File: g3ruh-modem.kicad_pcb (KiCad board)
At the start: 2 copper layers, 160 x 100 mm, 112 parts, among them P1 CONN_01X03, P2 CONN_01X06, P3 CONN_01X05, P4 C96ABC, Q1 LM7805_TO220, U1 4029, U10 LM339, U11 74HC14, U12 74HC164, U13 74HC86, U14 74HC164, U15 27C128, U16 TL084, U17 74HC74, U18 74HC164, U19 ZN429E-8, U2 27C128, U3 4029, U4 74HC164, U5 74HC74, U6 74HC86, U7 74HC164, U8 74HC161, U9 ZN429E-8

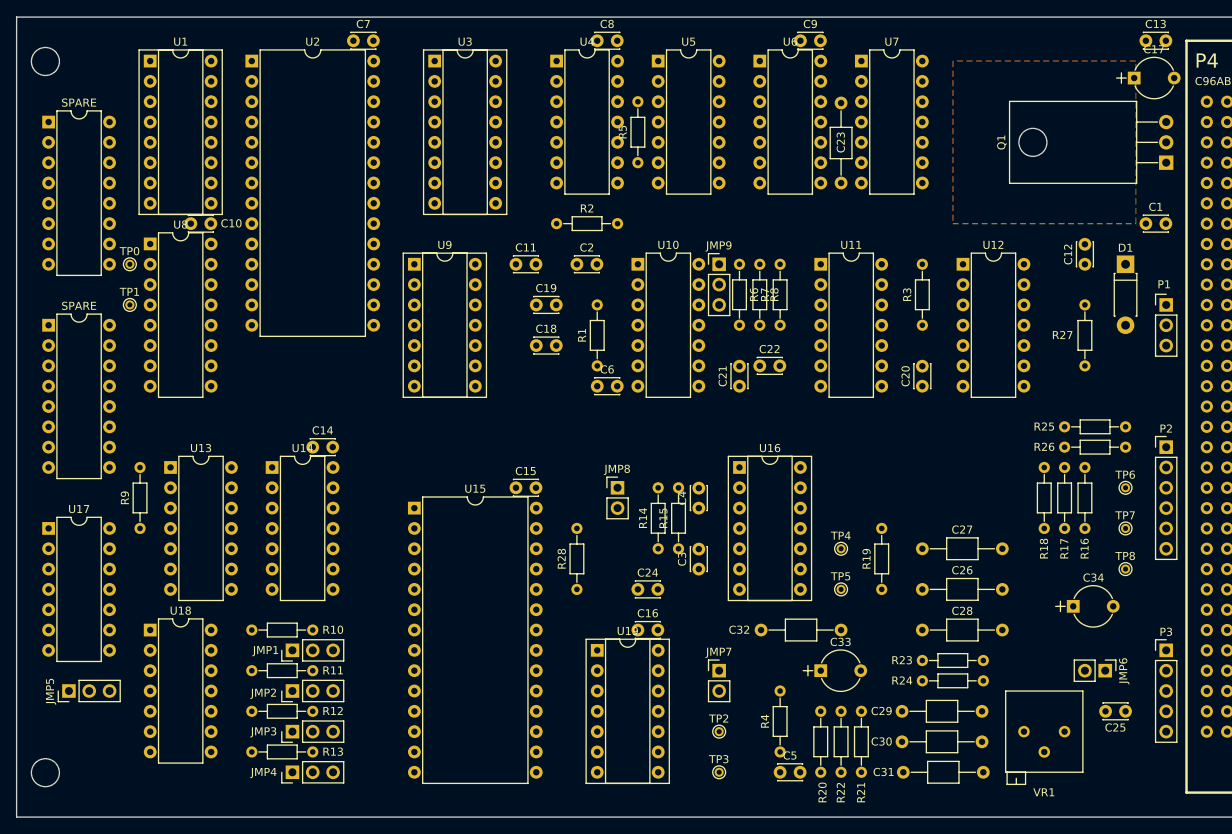
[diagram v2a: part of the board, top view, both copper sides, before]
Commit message: Final parts placement and verified net against an actual Issue 3 board.
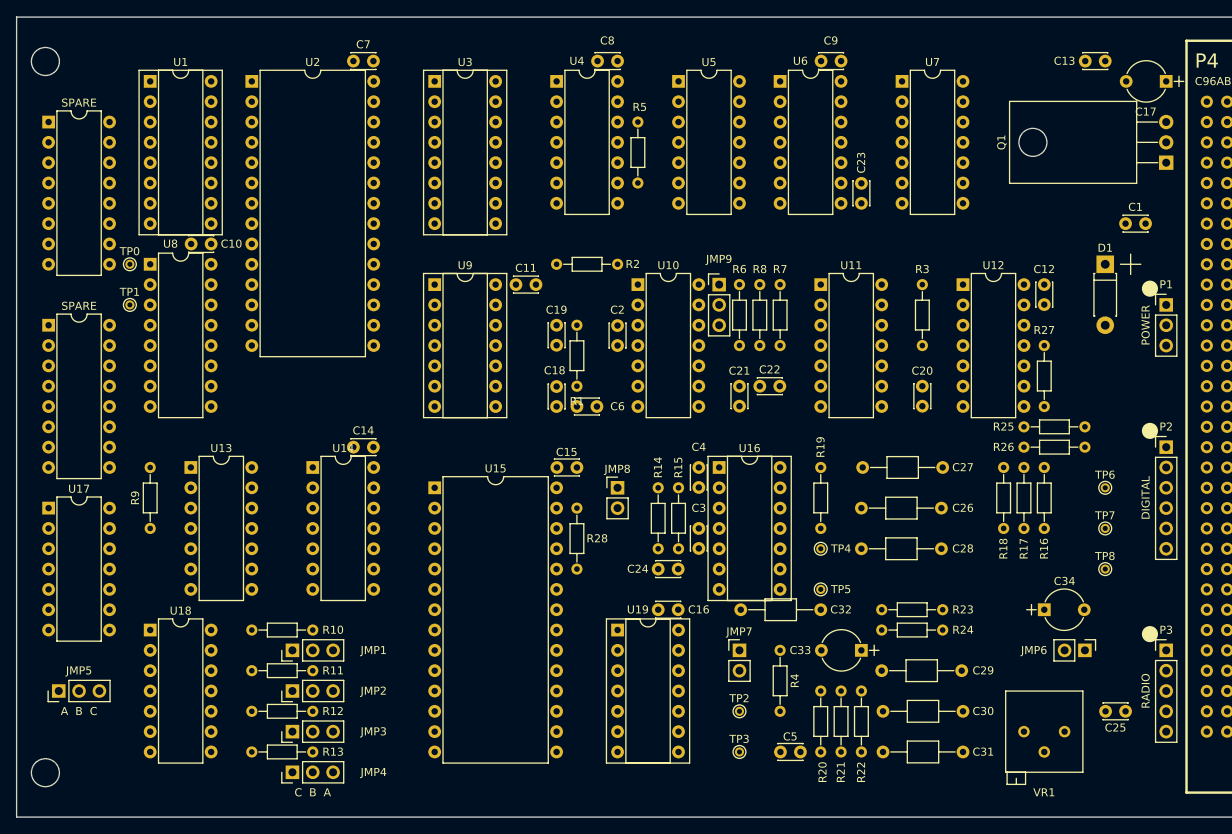
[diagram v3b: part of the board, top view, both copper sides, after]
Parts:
- C23: footprint Capacitors_THT:C_Axial_L3.8mm_D2.6mm_P10.00mm_Horizontal -> Capacitors_THT:C_Disc_D3.0mm_W2.0mm_P2.50mm
- C26: value 220p -> 220pF
- C29: value .0033 -> .0033uF
- R24: value 10K -> 12K
- moved C26 12.7 mm to (178.8, 104.8)
- moved C28 12.7 mm to (178.8, 109.8)
- moved R4 12.7 mm to (168.6, 122.5), turned to 270 degrees
- moved C2 11.4 mm to (148.3, 84.4), turned to 90 degrees
- moved R19 10.8 mm to (173.7, 107.3)
- moved C27 10.5 mm to (188.9, 99.7), turned to 180 degrees
- moved R28 10.2 mm to (143.2, 104.8), turned to 270 degrees
- moved R17 9.16 mm to (199.1, 99.7), turned to 270 degrees
- moved C30 8.52 mm to (191.4, 130.2), turned to 180 degrees
- moved R24 8.13 mm to (181.3, 120.0)
- moved R23 8.13 mm to (188.9, 117.5)
- moved C15 8.03 mm to (143.2, 99.7), turned to 180 degrees
- moved C18 8.03 mm to (140.7, 92.0), turned to 90 degrees
- moved R10 7.62 mm to (110.2, 120.0), turned to 180 degrees
- moved R11 7.62 mm to (110.2, 125.1), turned to 180 degrees
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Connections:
- net Net-(C29-Pad1) renamed /AUDIO OUT/DAC
- net Net-(R25-Pad2) renamed /ZERO CROSSING/TX_CLOCK
- net Net-(R5-Pad1) renamed /UNSCRAMBLER/RX_FILTER
- net Net-(U11-Pad1) renamed /LOCK_DETECT/ZERO_CROSSING
- net Net-(U11-Pad10) renamed /LOCK_DETECT/~RX_CLOCK
- net POWER renamed /CONNECTORS/POWER
- net U2_A3 renamed /RX CLOCK RECOVERY/U2_A3
- C15 pad 1: +5V -> GND
- C15 pad 2: GND -> +5V
- C16 pad 1: +5V -> GND
- C16 pad 2: GND -> +5V
- C18 pad 2: Vref -> VREF
- C2 pad 1: +12V -> GND
- C2 pad 2: GND -> +12V
- C25 pad 1: Net-(C25-Pad1) -> RX_AUDIO
- C25 pad 2: RX_AUDIO -> /RX FILTER/AUDIO_LOOPBACK_IN
- C26 pad 2: Vref -> VREF
- C28 pad 2: Vref -> VREF
- C29 pad 2: Vref -> VREF
- C30 pad 2: Vref -> VREF
- C4 pad 1: Vref -> VREF
- C5 pad 1: Vref -> VREF
- C6 pad 1: Vref -> VREF
- C7 pad 1: +5V -> GND
- C7 pad 2: GND -> +5V
- JMP6 pad 1: +5V -> /RX FILTER/AUDIO_LOOPBACK_IN
- JMP8 pad 1: Net-(JMP8-Pad1) -> GND
- JMP8 pad 2: GND -> Net-(JMP8-Pad2)
- R1 pad 2: Vref -> VREF
- R16 pad 1: Net-(C25-Pad1) -> /RX FILTER/AUDIO_LOOPBACK_IN
- R16 pad 2: Vref -> VREF
- R17 pad 2: Net-(C25-Pad1) -> /RX FILTER/AUDIO_LOOPBACK_IN
- R19 pad 2: Net-(C26-Pad1) -> Net-(C27-Pad2)
- R20 pad 1: Vref -> VREF
- R28 pad 1: Net-(JMP8-Pad1) -> Net-(JMP8-Pad2)
- U10 pad 12: GND -> VREF
- U10 pad 13: Net-(JMP9-Pad1) -> Net-(JMP9-Pad3)
- U10 pad 14: Net-(JMP9-Pad3) -> Net-(JMP9-Pad1)
- U10 pad 3: +5V -> +12V
- U10 pad 4: Vref -> VREF
- U10 pad 6: Vref -> VREF
- U15 pad 27: Net-(JMP8-Pad1) -> Net-(JMP8-Pad2)
- U16 pad 1: Vref -> VREF
- U16 pad 10: Vref -> VREF
- U16 pad 12: Net-(C27-Pad2) -> Net-(C26-Pad1)
- U16 pad 13: Net-(C26-Pad1) -> Net-(C27-Pad2)
- U16 pad 14: Net-(C26-Pad1) -> Net-(C27-Pad2)
- U16 pad 2: Vref -> VREF
- U6 pad 12: Net-(U12-Pad1) -> Net-(U6-Pad12)
- U6 pad 13: Net-(U6-Pad13) -> Net-(U12-Pad1)
- U7 pad 6: Net-(U6-Pad13) -> Net-(U6-Pad12)
- VR1 pad 1: Net-(C31-Pad1) -> VREF
- VR1 pad 3: Vref -> Net-(C31-Pad1)
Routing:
- removed copper zone on F.Cu, net GND

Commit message: Completed routing.
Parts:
- removed the REF** at (229.6, 137.8)
- removed the REF** at (229.6, 48.9)
- moved C14 2.54 mm to (117.8, 97.1), turned to 180 degrees
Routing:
- net GND: track 0.00 -> 940.6 mm
- net +5V: track 0.00 -> 575.9 mm
- net VREF: track 0.00 -> 192.3 mm
- net /ZERO CROSSING/TX_CLOCK: track 0.00 -> 155.0 mm, vias 0 -> 2
- net +12V: track 0.00 -> 138.1 mm, vias 0 -> 2
- net Net-(R26-Pad1): track 0.00 -> 131.1 mm
- net Net-(R2-Pad2): track 0.00 -> 99.9 mm
- net Net-(U1-Pad15): track 0.00 -> 97.4 mm, vias 0 -> 2
- net /LOCK_DETECT/~RX_CLOCK: track 0.00 -> 93.3 mm
- net Net-(U13-Pad11): track 0.00 -> 93.3 mm
- net DCD: track 0.00 -> 86.5 mm, vias 0 -> 1
- net Net-(U14-Pad13): track 0.00 -> 74.4 mm, vias 0 -> 1
- net Net-(C31-Pad1): track 0.00 -> 64.1 mm, vias 0 -> 1
- net Net-(U12-Pad1): track 0.00 -> 59.6 mm, vias 0 -> 2
- net /UNSCRAMBLER/RX_FILTER: track 0.00 -> 58.3 mm
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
